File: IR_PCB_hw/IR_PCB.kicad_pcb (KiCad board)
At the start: 4 copper layers, 49.5 x 49 mm, 128 parts, among them Q1 M28S, Q10 SI2301, Q11 SI2301, Q2 M28S, Q3 TSOP4856, Q4 TSOP4856, Q5 SI2301, Q6 TSOP4856, Q7 SI2301, Q8 SI2301, Q9 SI2301

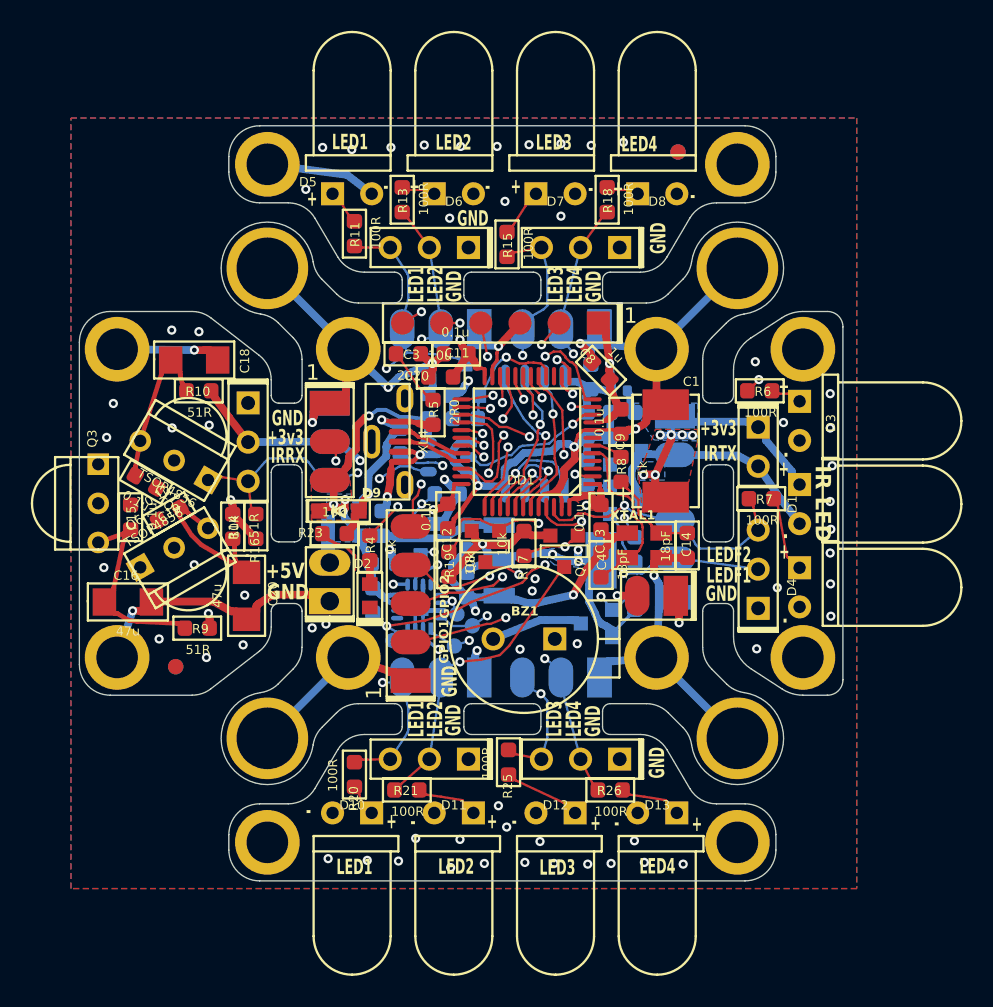
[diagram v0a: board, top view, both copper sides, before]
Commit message: Switching to CDC+MSD
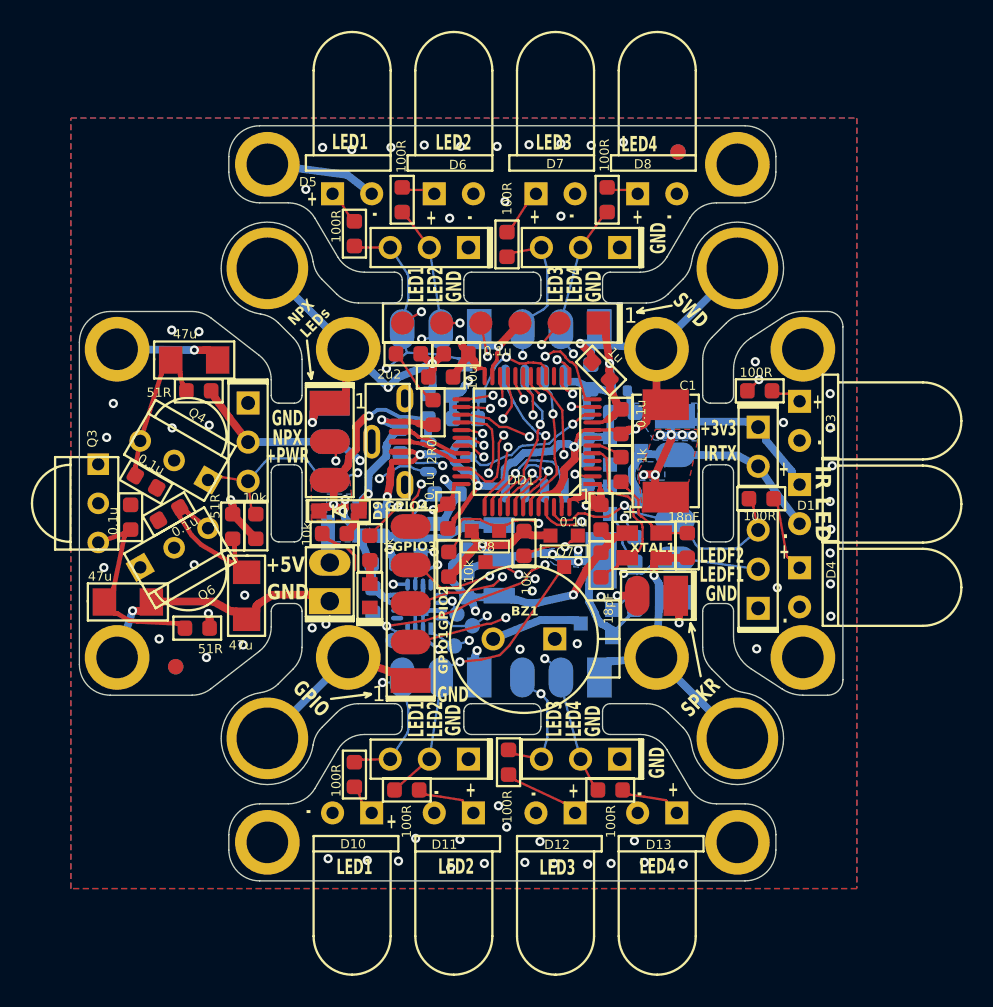
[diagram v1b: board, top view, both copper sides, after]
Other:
- board text added: "+PWR"
- board text added: "GPIO"
- board text added: "GPIO3"
- board text added: "GPIO4"
- board text added: "IR_PCB v3.2"
- board text added: "NPX"
- board text added: "NPX LEDs"
- board text added: "SPKR"
- board text added: "SWD"
